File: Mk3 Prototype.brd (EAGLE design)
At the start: 113 x 55.2 mm, 183 parts, among them IC1 BD49XXX, IC2 CC3100, IC3 S25FL216K0PMFI011, IC4 STM32F401V, IC6 AP3419, J1 ZX62-AB-5PA(11), J2 SWD_SHROUD, J7 SFV30R-2STE1HLF, Q1 BSS84W, Q11 BSS84W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

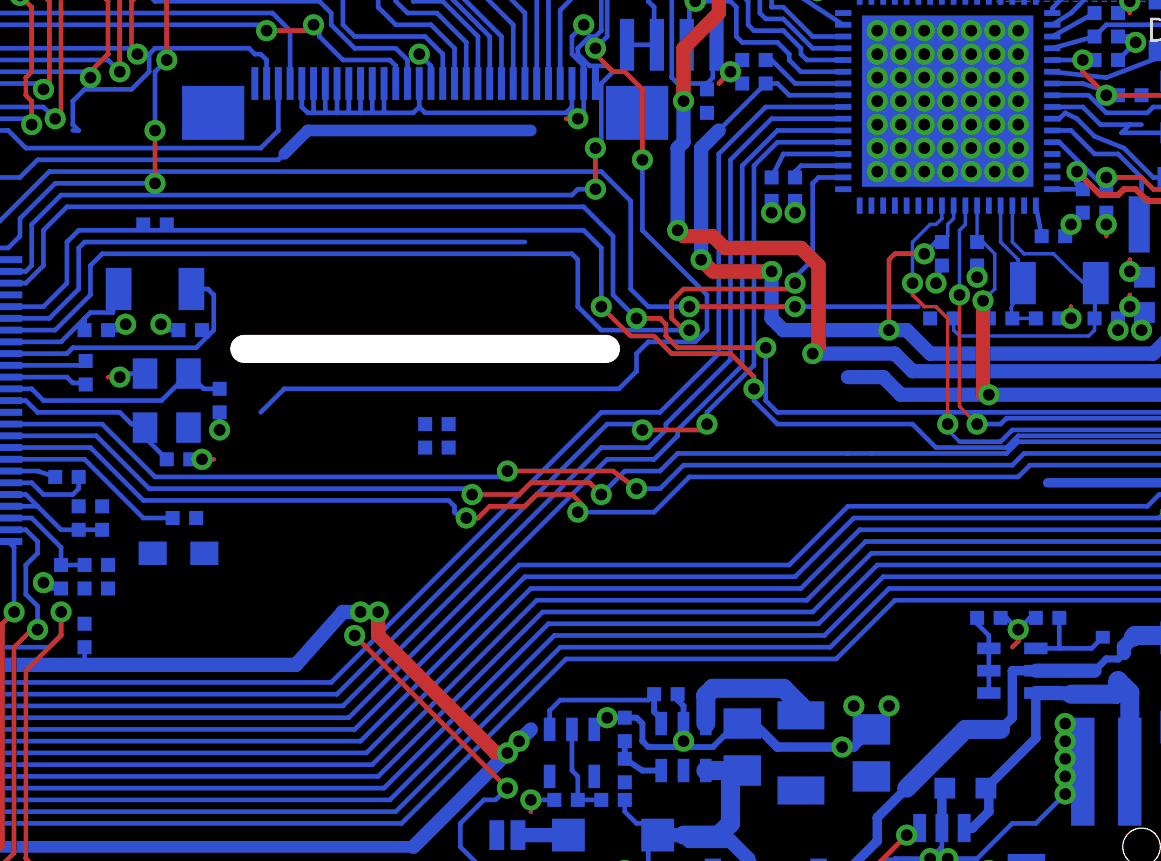
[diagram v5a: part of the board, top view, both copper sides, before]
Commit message: redone some of the cc spi routing
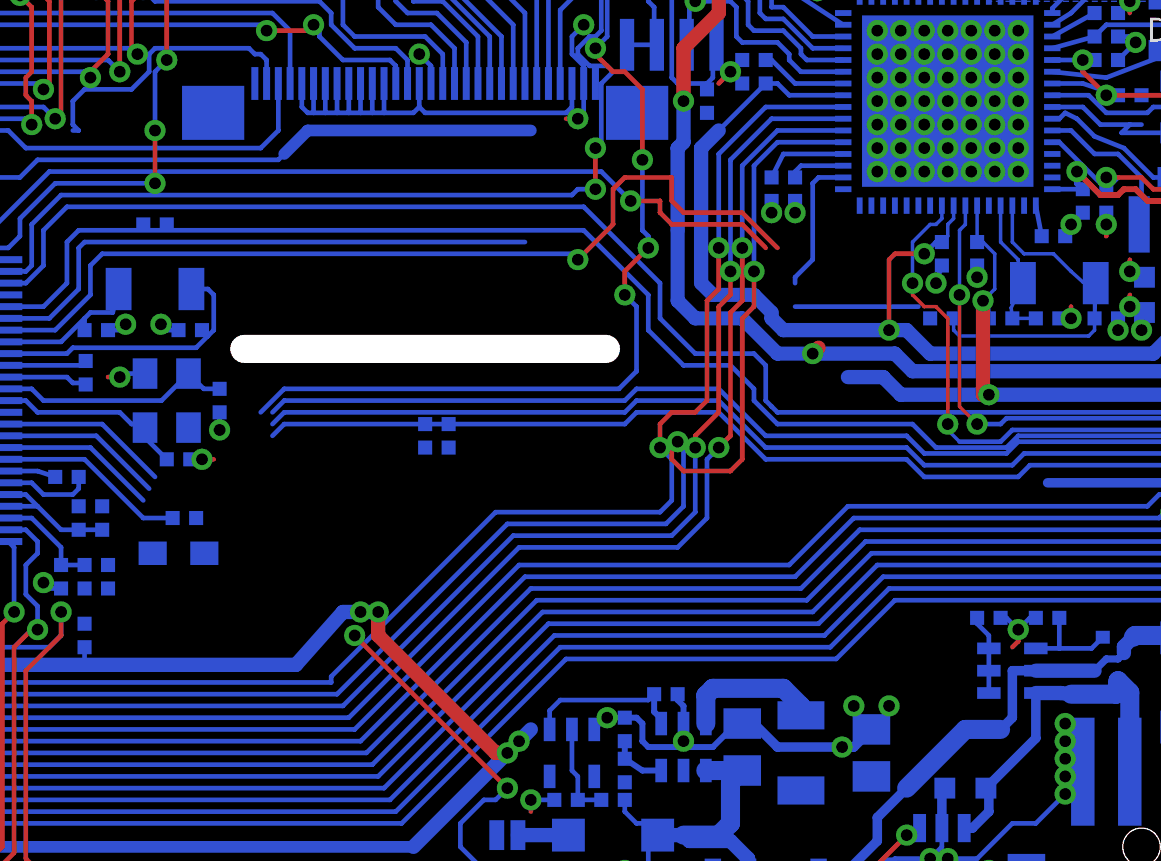
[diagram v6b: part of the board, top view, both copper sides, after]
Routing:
- net ESP_GPIO16: track 70.8 -> 64.5 mm, vias 2 -> 0
- net SPI1_SCK: track 58.4 -> 63.7 mm
- net ESP_GPIO0: track 72.5 -> 67.6 mm, vias 2 -> 0
- net ESP_CH_PD: track 71.0 -> 66.8 mm, vias 2 -> 0
- net MCO1: track 63.9 -> 59.8 mm, vias 2 -> 1
- net SPI1_NSS: track 57.4 -> 61.1 mm, vias 0 -> 2
- net AREF: track 61.8 -> 58.9 mm, vias 3 -> 5
- net SPI1_MOSI: track 60.4 -> 63.1 mm, vias 0 -> 2
- net SPI1_MISO: track 59.5 -> 62.3 mm, vias 0 -> 2
- net WIFI_!HIB: track 46.8 -> 45.1 mm, vias 2 -> 1
- net MOM_UP: track 83.0 -> 81.7 mm, vias 3 -> 1
- net SPI4_MOSI: track 94.5 -> 93.6 mm, vias 3 -> 1
- net N$22: track 51.1 -> 50.7 mm, vias 4 -> 2
- net N$18: track 92.1 -> 91.7 mm, vias 8 -> 7

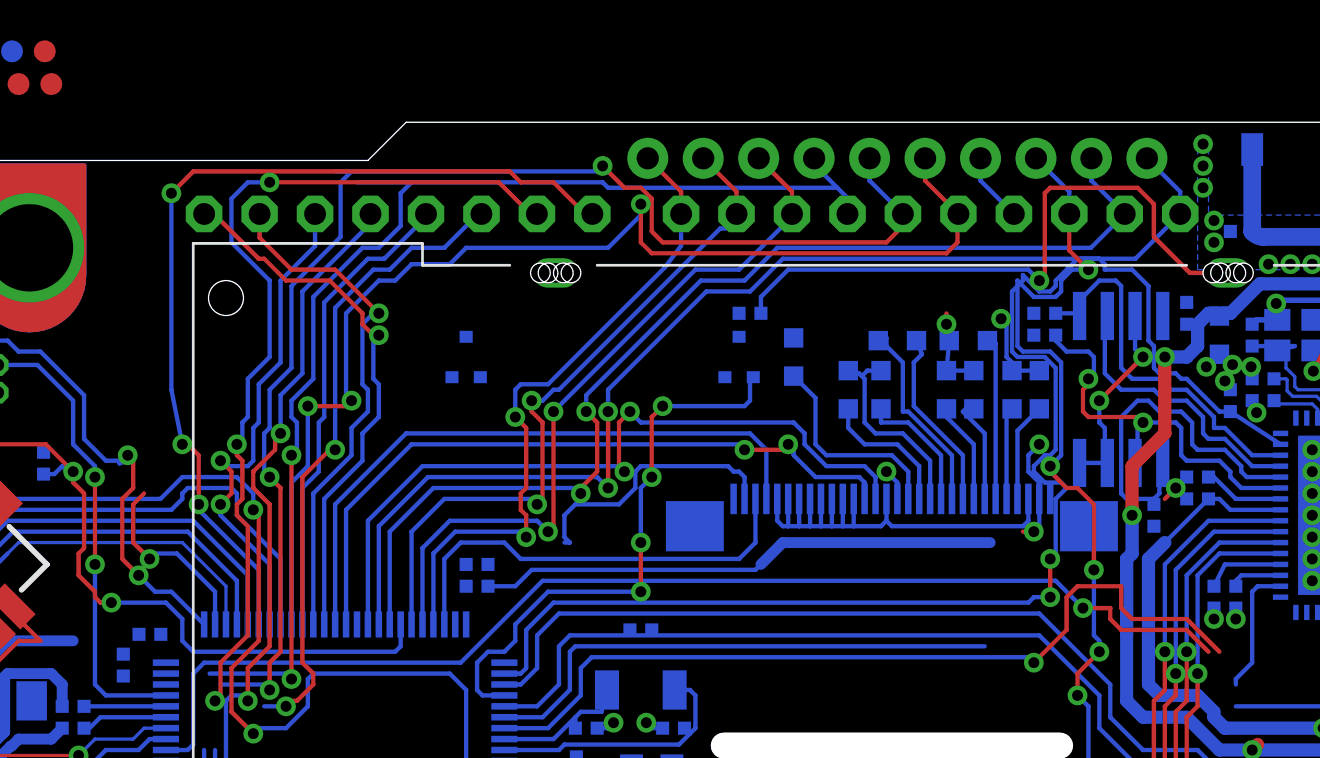
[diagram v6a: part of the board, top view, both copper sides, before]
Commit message: moved routing a little
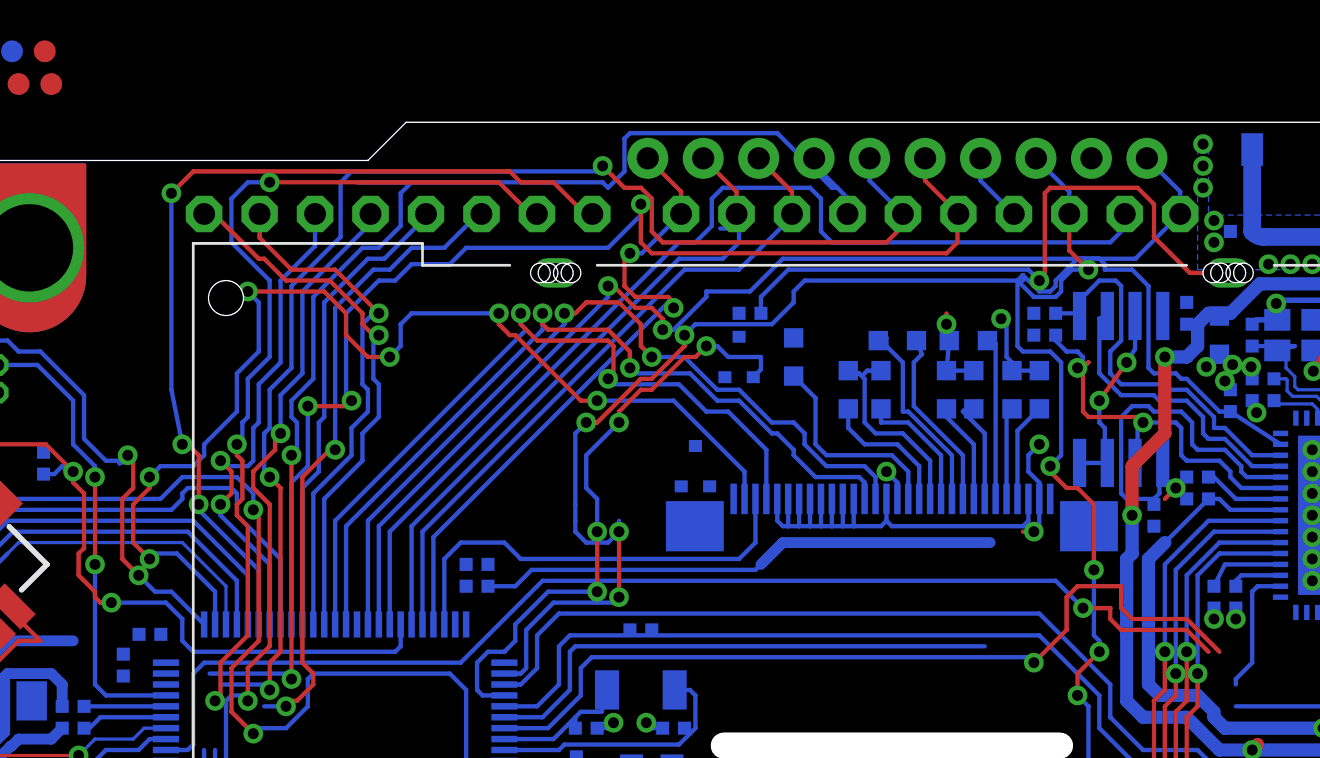
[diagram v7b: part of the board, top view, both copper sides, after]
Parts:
- moved Q11 11.6 mm to (47.5, 39.5)
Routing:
- net SPI3_NSS: track 21.3 -> 51.9 mm, vias 1 -> 6
- net LCD_A0: track 29.2 -> 35.7 mm, vias 0 -> 2
- net SPI3_SCK: track 32.1 -> 37.6 mm
- net WIFI_INTR: track 64.3 -> 61.0 mm, vias 2 -> 4
- net TIM11_CH1: track 33.8 -> 30.5 mm, vias 2 -> 0
- net SPI3_MOSI: track 34.5 -> 37.6 mm
- net SPI2_MOSI: track 56.2 -> 59.1 mm
- net I2C_SDA: track 50.2 -> 48.0 mm, vias 2 -> 0
- net TIM9_CH1: track 26.0 -> 28.2 mm
- net TIM10_CH1: track 32.3 -> 30.2 mm, vias 2 -> 0
- net CC_FLASH_!CS: track 17.2 -> 18.1 mm
- net I2C_SCL: track 53.4 -> 52.7 mm

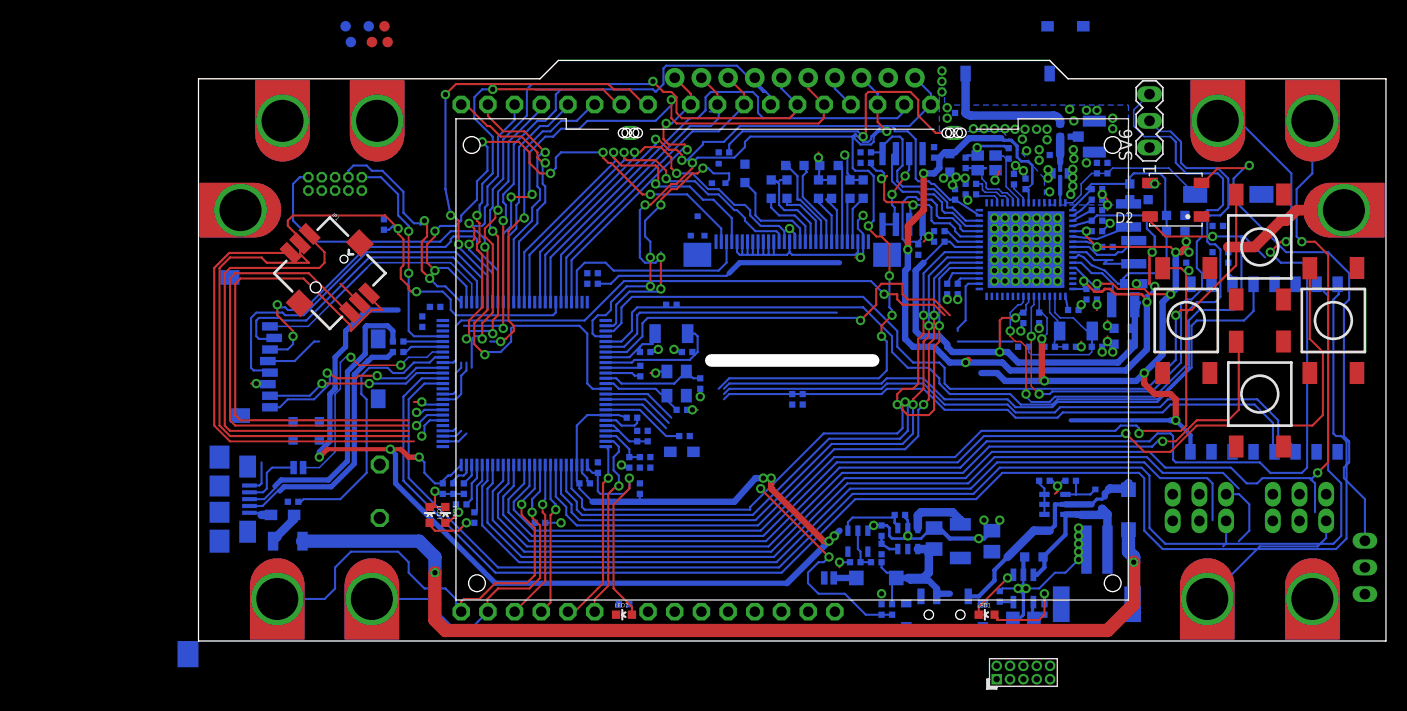
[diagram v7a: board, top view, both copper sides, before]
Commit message: improving routing around usb
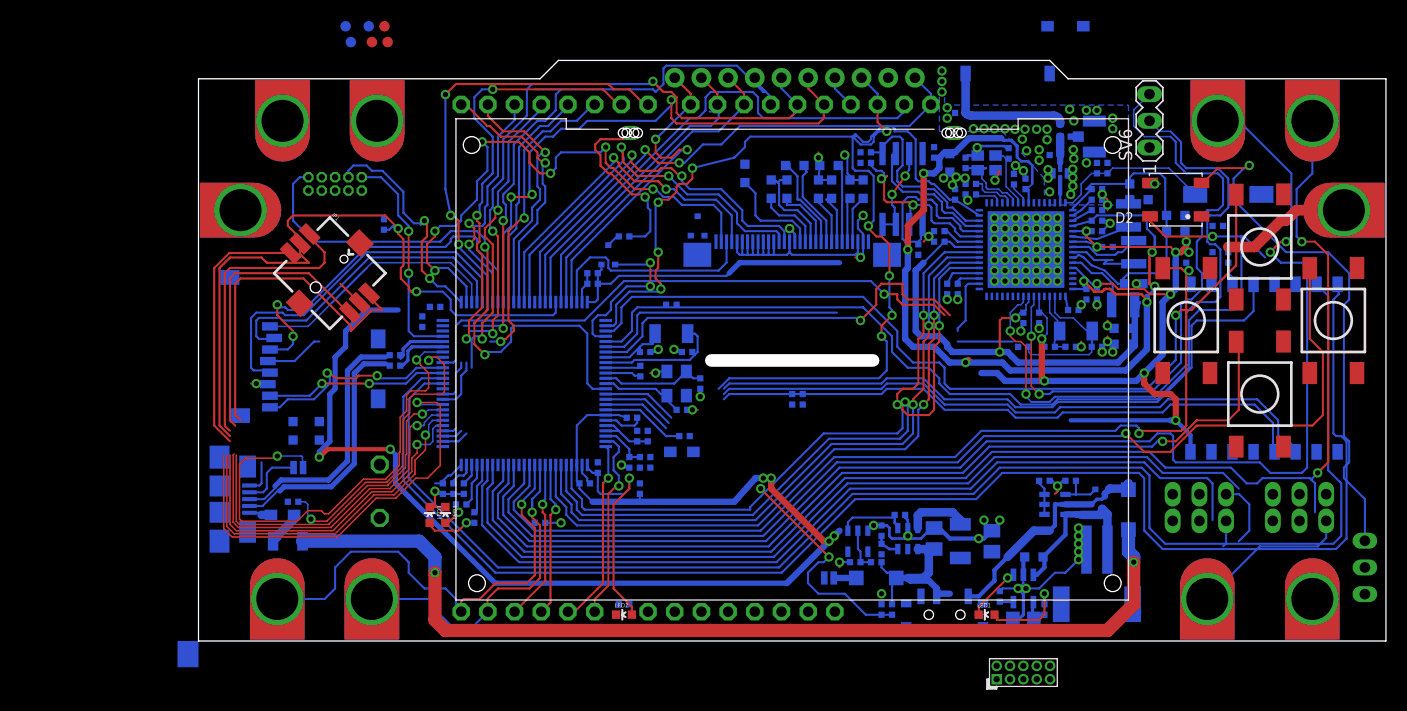
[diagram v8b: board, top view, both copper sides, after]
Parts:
- removed Q12: 2N7002KW, TiLDA Mk3 Parts:SC70-3-R
- added Q2: BSS84W, TiLDA Mk3 Parts:SC70-3-R
- moved R45 12.4 mm to (40.5, 38.5)
- moved R15 1.33 mm to (18.7, 26.2)
- moved R16 1.33 mm to (18.7, 27.2)
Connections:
- removed net LCD_A_SWITCHED: Q12.3, R45.2
- new net N$57: Q2.3, R45.2
- net +3V3: now also Q2.2; no longer U2.A
- net GND: now also U2.K; no longer Q12.2
- net N$1: now also U2.A; no longer U2.K
- net TIM9_CH1: now also Q2.1; no longer Q12.1
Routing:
- net USB_ID_: track 23.2 -> 45.6 mm
- net JOY_DWN: track 46.7 -> 68.7 mm
- net JOY_RIGHT: track 42.5 -> 58.2 mm, vias 0 -> 1
- net JOY_LEFT: track 51.8 -> 65.8 mm
- net BOOT0: track 86.6 -> 100.4 mm
- net JOY_UP: track 48.6 -> 62.0 mm
- net TIM9_CH1: track 28.2 -> 15.6 mm, vias 4 -> 2
- net N$1: track 29.3 -> 17.2 mm
- net USB_D_P: track 28.4 -> 24.3 mm
- net FS_VUSB: track 26.0 -> 29.9 mm, vias 0 -> 2
- net WIFI_INTR: track 61.0 -> 57.6 mm
- net GND: track 125.1 -> 128.1 mm
- net LCD_A0: track 35.7 -> 33.7 mm
- net SPI3_NSS: track 51.9 -> 53.8 mm
- net D8: track 30.2 -> 32.0 mm
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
